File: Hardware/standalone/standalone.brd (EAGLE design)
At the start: 100 x 80 mm, 87 parts, among them Q2 32.768khz, U1 DMS3016SSS-13, U2 DMS3016SSS-13, U3 DMS3016SSS-13, U4 LM2575S-15, U5 NMOS_2N7002, U6 NMOS_2N7002, X1 KUSBVX, X2 KUSBVX

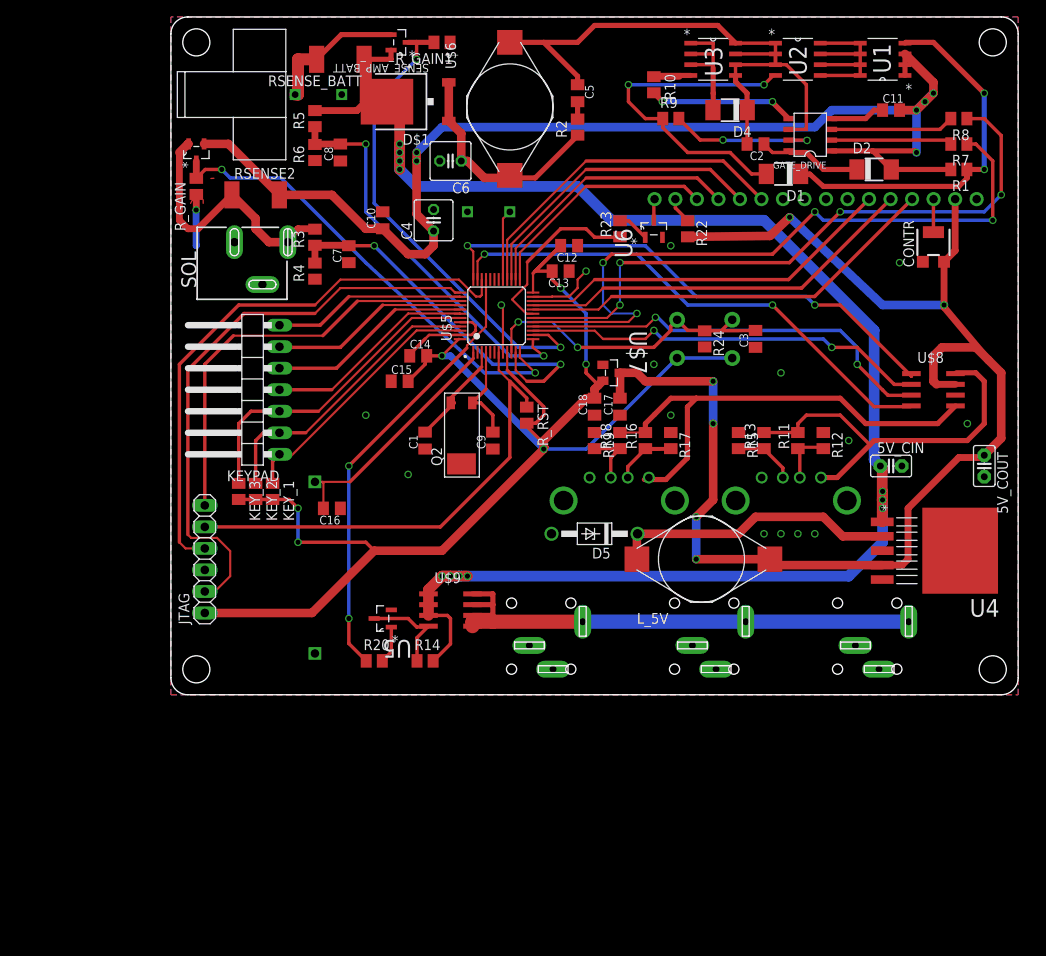
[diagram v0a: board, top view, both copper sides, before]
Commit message: Some Hardware Fixes
Fixed the Battery Connector.
Added more items to ToDo list
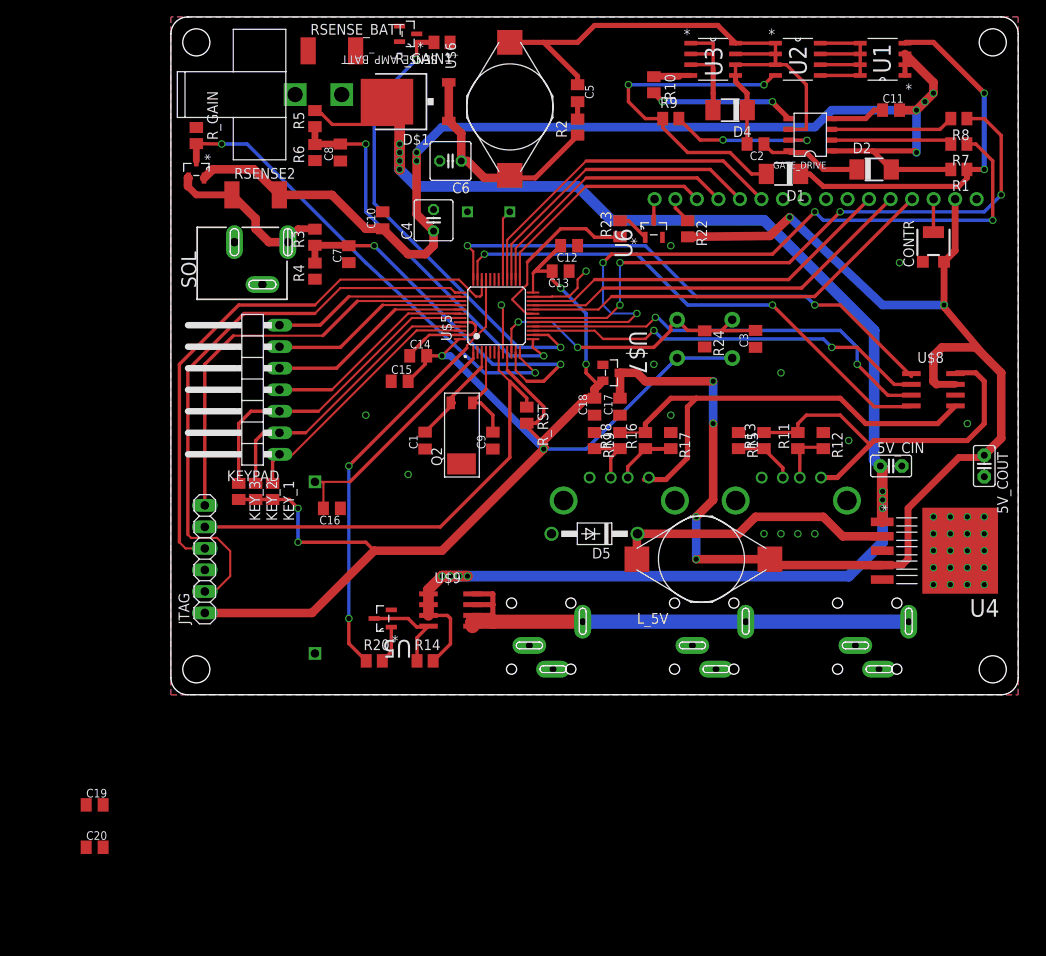
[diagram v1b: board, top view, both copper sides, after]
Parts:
- added C19: 1uF, resistor:C0805K
- added C20: 10uF, resistor:C0805K
- C7: value 0.1uF -> 10uF
- C8: value 0.1uF -> 1uF
- R_GAIN, R_GAIN1: value 10K -> 1k65
- moved R_GAIN 6.00 mm to (3.00, 66.0), turned to 270 degrees
- moved SENSE_AMP_SOL 2.00 mm to (3.00, 62.0), turned to 270 degrees
- moved RSENSE_BATT 1.41 mm to (19.0, 76.0), turned to 0 degrees
- moved SENSE_AMP_BATT 1.41 mm to (28.0, 78.0)
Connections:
- net BATT_I: now also C20.2
- net GND: now also C19.1, C20.1
- net SOL_I: now also C19.2
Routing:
- net N$4: track 16.7 -> 0.00 mm
- net N$16: track 31.5 -> 20.4 mm
- net GND: track 57.0 -> 48.4 mm, vias 16 -> 20
- net V_LOAD: track 195.7 -> 190.7 mm
- net BATT_I: track 57.0 -> 56.0 mm
- net SOL_I: track 55.3 -> 56.2 mm
- net N$9: track 148.4 -> 147.6 mm

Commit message: Cleaned Library and Complete some ToDo list
Added power LED and changed MPPT reverse current diode
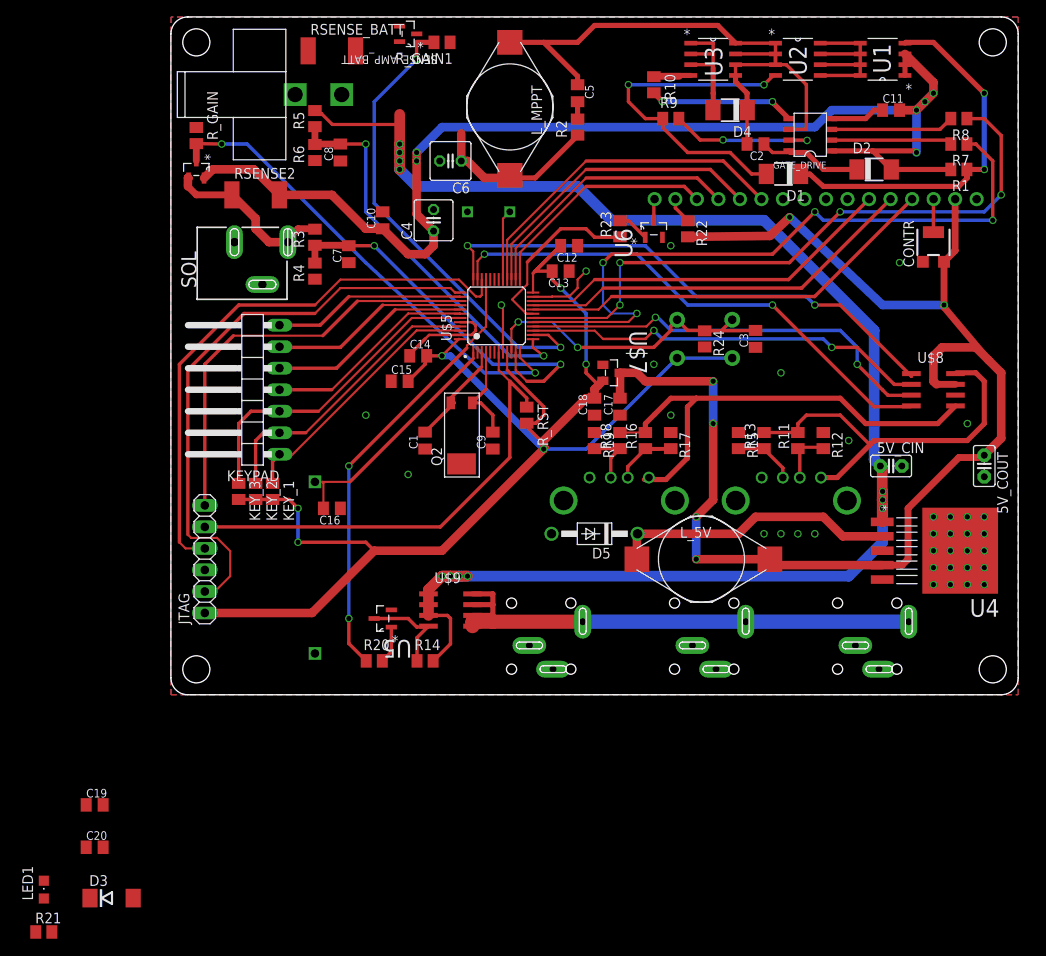
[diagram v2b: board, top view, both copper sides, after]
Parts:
- removed D$1: (no value), equinox:TO252
- removed U$6: 330uF, lib:BOURNS_SDR1806
- added D3: (no value), equinox:DO214AA
- added LED1: (no value), led:CHIPLED_0805
- added L_MPPT: 330u, equinox:BOURNS_SDR1806
- added R21: (no value), resistor:M0805
- L_5V: value 330uF -> 330u; device lib:BOURNS_SDR1806 -> equinox:BOURNS_SDR1806
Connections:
- new net N$37: LED1.C, R21.2
- net +3V3: now also LED1.A
- net GND: now also R21.1
- net N$12: now also D3.A, L_MPPT.P$2; no longer D$1.1, D$1.2, U$6.P$2
- net N$6: now also L_MPPT.P$1; no longer U$6.P$1
- net V_LOAD: now also D3.C; no longer D$1.3
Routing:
- net N$12: track 27.0 -> 20.4 mm
- net V_LOAD: track 190.7 -> 185.6 mm
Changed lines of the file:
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@@
 <layer number="24" name="bOrigins" color="15" fill="1" visible="yes" active="yes"/>
 <layer number="25" name="tNames" color="7" fill="1" visible="yes" active="yes"/>
-<layer number="26" name="bNames" color="7" fill="1" visible="no" active="yes"/>
+<layer number="26" name="bNames" color="7" fill="1" visible="yes" active="yes"/>
 <layer number="27" name="tValues" color="7" fill="1" visible="yes" active="yes"/>
-<layer number="28" name="bValues" color="7" fill="1" visible="no" active="yes"/>
+<layer number="28" name="bValues" color="7" fill="1" visible="yes" active="yes"/>
 <layer number="29" name="tStop" color="7" fill="3" visible="no" active="yes"/>
 <layer number="30" name="bStop" color="7" fill="6" visible="no" active="yes"/>
@@
 <element name="R10" library="rcl" package="M0805" value="5" x="57" y="72" rot="R270"/>
 <element name="C11" library="resistor" package="C0805K" value="1uF" x="85" y="69"/>
-<element name="U$6" library="lib" package="BOURNS_SDR1806" value="330uF" x="40" y="77" rot="R270"/>
+<element name="L_MPPT" library="equinox" package="BOURNS_SDR1806" value="330u" x="40" y="77" rot="R270"/>
 <element name="SENSE_AMP_SOL" library="equinox" package="SOT91P240X110-3N" value="ZXCT1107SA-7" x="3" y="62" smashed="yes" rot="R270">
 <attribute name="PACKAGE" value="SOT-23-3" x="-92" y="102" size="1.778" layer="27" rot="R270" display="off"/>
@@
 </element>
 <element name="D4" library="diode" package="DO-214AC" value="US1D - 1625280" x="66" y="69" rot="R180"/>
-<element name="D$1" library="equinox" package="TO252" value="" x="28" y="70" rot="R90"/>
 <element name="SOL" library="equinox" package="POWER_JACK_SLOT" value="POWER_JACK_2.1MMSLT" x="0" y="56" smashed="yes" rot="R270">
 <attribute name="NAME" x="3" y="48" size="1.778" layer="25" rot="R90"/>
@@
 <attribute name="VALUE" x="79.8428" y="22.5372" size="2.0828" layer="27" ratio="10" rot="SR270"/>
 </element>
-<element name="L_5V" library="lib" package="BOURNS_SDR1806" value="330uF" x="55" y="16">
+<element name="L_5V" library="equinox" package="BOURNS_SDR1806" value="330u" x="55" y="16">
 <attribute name="VERSION" value="0.1" x="55" y="16" size="1.778" layer="27" display="off"/>
 <attribute name="AUTHOR" value="Ashley Grealish" x="55" y="16" size="1.778" layer="27" display="off"/>
@@
 <attribute name="AUTHOR" value="Ashley Grealish" x="-9" y="-18" size="1.778" layer="27" display="off"/>
 </element>
+<element name="D3" library="equinox" package="DO214AA" value="" x="-7" y="-24"/>
+<element name="LED1" library="led" package="CHIPLED_0805" value="" x="-15" y="-23"/>
+<element name="R21" library="resistor" package="M0805" value="" x="-15" y="-28"/>
 </elements>
 <signals>
@@
 <contactref element="C19" pad="1"/>
 <contactref element="C20" pad="1"/>
+<contactref element="R21" pad="1"/>
 <wire x1="88.75" y1="51.1" x2="95.1" y2="58.5" width="0" layer="19" extent="1-1"/>
 <wire x1="86" y1="51" x2="88.75" y2="51.1" width="0" layer="19" extent="1-1"/>
@@
 <wire x1="-10" y1="-13" x2="4" y2="14.73" width="0" layer="19" extent="1-1"/>
 <wire x1="-10" y1="-18" x2="-10" y2="-13" width="0" layer="19" extent="1-1"/>
+<wire x1="-15.95" y1="-28" x2="-10" y2="-18" width="0" layer="19" extent="1-1"/>
 </signal>
 <signal name="N$5">
@@
 <contactref element="C2" pad="2"/>
 <contactref element="C5" pad="1"/>
-<contactref element="U$6" pad="P$1"/>
+<contactref element="L_MPPT" pad="P$1"/>
 <contactref element="GATE_DRIVE" pad="6"/>
 <contactref element="D4" pad="C"/>
@@
 <contactref element="RSENSE_BATT" pad="1"/>
 <contactref element="SENSE_AMP_BATT" pad="3"/>
-<contactref element="D$1" pad="3"/>
 <contactref element="U$9" pad="1"/>
 <contactref element="U$9" pad="3"/>
@@
 <wire x1="34.29" y1="14" x2="34" y2="14" width="1.27" layer="16"/>
 <wire x1="34" y1="14" x2="32" y2="14" width="1.27" layer="16"/>
-<wire x1="27" y1="68.5" x2="25.5" y2="70" width="1.27" layer="1"/>
 <wire x1="27" y1="68.5" x2="27" y2="65" width="1.27" layer="1"/>
 <via x="27" y="62" extent="1-16" drill="0.6"/>
@@
 <wire x1="26.67" y1="67.31" x2="19.05" y2="67.31" width="0.381" layer="1"/>
 <wire x1="17.78" y1="68.58" x2="17" y2="68.95" width="0.381" layer="1"/>
-<wire x1="26.67" y1="67.31" x2="25.5" y2="70" width="0.381" layer="1"/>
-<wire x1="16.2" y1="76" x2="26.984" y2="78.9144" width="0" layer="19" extent="1-1"/>
-<wire x1="25.5" y1="70" x2="16.2" y2="76" width="0" layer="19" extent="1-1"/>
+<contactref element="D3" pad="C"/>
+<wire x1="27" y1="68.5" x2="26.984" y2="78.9144" width="0" layer="19" extent="1-1"/>
+<wire x1="26.67" y1="67.31" x2="27" y2="68.5" width="0" layer="19" extent="1-1"/>
+<wire x1="16.2" y1="76" x2="17" y2="68.95" width="0" layer="19" extent="1-1"/>
+<wire x1="-9.55" y1="-24" x2="30.95" y2="4" width="0" layer="19" extent="1-1"/>
 </signal>
 <signal name="N$12">
-<contactref element="D$1" pad="1"/>
-<contactref element="D$1" pad="2"/>
 <contactref element="R2" pad="1"/>
-<contactref element="U$6" pad="P$2"/>
+<contactref element="L_MPPT" pad="P$2"/>
 <contactref element="C6" pad="1"/>
 <wire x1="48" y1="66.05" x2="48" y2="66" width="0.6096" layer="1"/>
@@
 <wire x1="39.6972" y1="61" x2="40" y2="61.3028" width="1.016" layer="1"/>
 <wire x1="34.27" y1="63" x2="34.27" y2="66.25" width="1.016" layer="1"/>
-<wire x1="34.27" y1="66.25" x2="32.8" y2="67.72" width="1.016" layer="1"/>
-<wire x1="32.8" y1="72.28" x2="32.8" y2="67.72" width="1.016" layer="1"/>
+<contactref element="D3" pad="A"/>
+<wire x1="-4.45" y1="-24" x2="37" y2="61" width="0" layer="19" extent="1-1"/>
 </signal>
 <signal name="USB_OUT2" class="1">
@@
 <wire x1="45" y1="50" x2="45" y2="49" width="0.4064" layer="1"/>
 <wire x1="45" y1="49" x2="46" y2="48" width="0.4064" layer="1"/>
+<contactref element="LED1" pad="A"/>
+<wire x1="4" y1="9.65" x2="-15" y2="-24.05" width="0" layer="19" extent="1-1"/>
 </signal>
 <signal name="+5V">
@@
 <via x="96" y="13" extent="1-16" drill="0.6"/>
 </signal>
+<signal name="N$37">
+<contactref element="LED1" pad="C"/>
+<contactref element="R21" pad="2"/>
+<wire x1="-15" y1="-21.95" x2="-14.05" y2="-28" width="0" layer="19" extent="1-1"/>
+</signal>
 </signals>

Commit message: Many PCB Improvements
Tidied up Silkscreen.
Changed some through hole components to surface mount.
Changed the 15V regulator for 5V as originally intended.
Checked power rating of converters. Need to update 5V out to 3A.
On PCB, tidied up the 12V track and thickened so that it can carry
larger current.
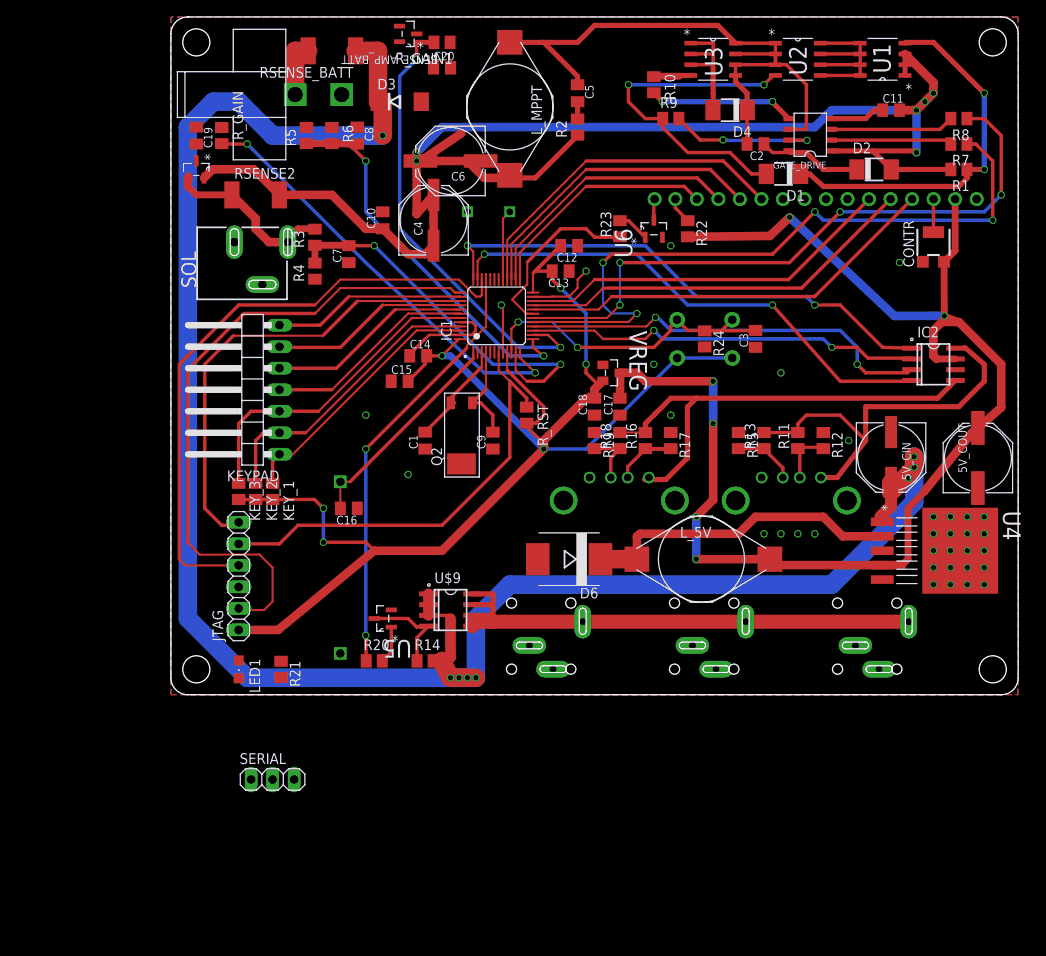
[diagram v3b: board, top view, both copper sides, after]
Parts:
- removed D5: (no value), diode:DO41Z10
- removed U$8: AP1212, equinox:SO8
- added D6: B340-13-F, equinox:SMC
- added IC2: AP1212, equinox:SO8
- added SERIAL: (no value), pinhead:1X03
- 5V_CIN: device capacitor-wima:C2.5-2 -> resistor:PANASONIC_E
- 5V_COUT: device capacitor-wima:C2.5-2 -> resistor:PANASONIC_F
- C4: device resistor:C025-050X050 -> resistor:PANASONIC_E
- C6: device resistor:C025-050X050 -> resistor:PANASONIC_F
- LED1: value (none) -> POW_3V3
- R21: value (none) -> 1K
- U4: value LM2575S-15 -> LM2575S-5
- moved C20 100.7 mm to (32.0, 74.0)
- moved D3 100.0 mm to (27.0, 70.0)
- moved C19 79.9 mm to (3.00, 66.0), turned to 270 degrees
- moved R21 41.8 mm to (13.0, 3.00), turned to 270 degrees
- moved LED1 34.7 mm to (8.00, 3.00), turned to 180 degrees
- moved JTAG 4.47 mm to (8.00, 14.0)
- moved BATT_BCKUP 3.00 mm to (20.0, 15.0)
- moved R_GAIN 3.00 mm to (6.00, 66.0)
- moved C8 2.83 mm to (22.0, 66.0), turned to 270 degrees
- moved R6 2.83 mm to (19.0, 66.0), turned to 270 degrees
- moved R5 2.24 mm to (16.0, 66.0)
- moved C16 2.00 mm to (21.0, 22.0)
- moved 5V_COUT 1.20 mm to (95.2, 27.9), turned to 90 degrees
- moved 5V_CIN 1.00 mm to (85.0, 28.0), turned to 270 degrees
- turned RSENSE_BATT to 180 degrees
- renumbered U$5 to IC1, U$7 to VREG
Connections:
- net +5V: now also 5V_COUT.+, IC2.7; no longer 5V_COUT.1, U$8.7
- net GND: now also 5V_CIN.-, 5V_COUT.-, C4.-, C6.-, D6.A, IC2.6, SERIAL.3; no longer 5V_CIN.2, 5V_COUT.2, C4.2, C6.2, D5.A, U$8.6
- net N$12: now also C6.+; no longer C6.1
- net N$21: now also D6.C; no longer D5.C
- net N$9: now also C4.+; no longer C4.1
- net USART1_RX: now also SERIAL.1
- net USART1_TX: now also SERIAL.2
- net USB_EN1: now also IC2.1; no longer U$8.1
- net USB_EN2: now also IC2.4; no longer U$8.4
- net USB_FLG1: now also IC2.2; no longer U$8.2
- net USB_FLG2: now also IC2.3; no longer U$8.3
- net USB_OUT1: now also IC2.8; no longer U$8.8
- net USB_OUT2: now also IC2.5; no longer U$8.5
- net V_LOAD: now also 5V_CIN.+; no longer 5V_CIN.1
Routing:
- net V_LOAD: track 185.6 -> 232.7 mm, vias 11 -> 8
- net SWCLK: track 68.3 -> 76.5 mm
- net N$12: track 20.4 -> 27.7 mm
- net N$4: track 0.00 -> 6.70 mm
- net SWO: track 49.9 -> 56.5 mm
- net SWDIO: track 66.9 -> 72.9 mm
- net SOL_I: track 56.2 -> 51.1 mm
- net +5V: track 162.5 -> 157.9 mm
- net N$9: track 147.6 -> 152.1 mm
- net N$21: track 33.7 -> 37.9 mm
- net +3V3: track 179.9 -> 176.2 mm
- net NRST: track 56.2 -> 53.1 mm
- net V_BACKUP: track 29.5 -> 26.3 mm
- net BATT_I: track 56.0 -> 53.5 mm
- net USB_EN1: track 63.3 -> 61.6 mm
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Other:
- board text added: "Move Buzzer Swap Solar and Batt Connector"
- board text removed: "INNER BOX DIMENSIONS"
- board text removed: "KEYPAD"
- board text removed: "OUTER BOX DIMENSIONS"

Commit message: Increase 5V Output to 3A max
Switched SMPS Controller, Inductor and Capacitor.
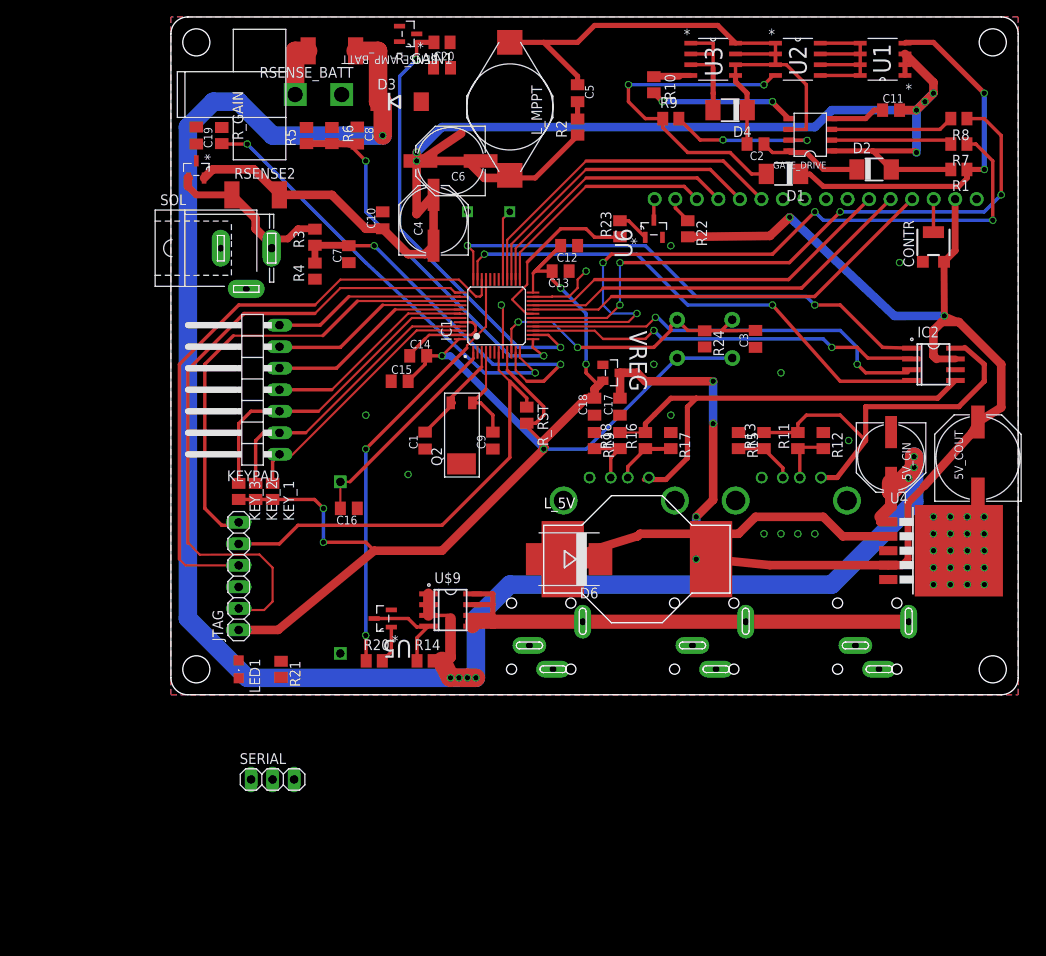
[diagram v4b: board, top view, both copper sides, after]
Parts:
- 5V_COUT: value 330u -> 1000uF; device resistor:PANASONIC_F -> resistor:PANASONIC_G
- L_5V: value 330u -> 100uH; device equinox:BOURNS_SDR1806 -> equinox:INDUC_BOURNS_SDR2207
- L_MPPT: device equinox:BOURNS_SDR1806 -> equinox:INDUC_BOURNS_SDR1806
- SOL: value POWER_JACK_2.1MMSLT -> (none); device equinox:POWER_JACK_SLOT -> con-jack:SPC4077
- U4: value LM2575S-5 -> LM2576S; device equinox:TO170P1435X465-6N -> equinox:TO263-5
- moved SOL 9.48 mm to (8.89, 52.7), turned to 0 degrees
- moved U4 2.54 mm to (90.5, 17.0)
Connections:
- net GND: now also SOL.1, SOL.2; no longer SOL.GND@1, SOL.GND@2
- net N$16: now also SOL.3; no longer SOL.PWR
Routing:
- net N$21: track 37.9 -> 45.2 mm
- net N$16: track 20.4 -> 21.2 mm
- net V_LOAD: track 232.7 -> 233.4 mm
- net +5V: track 157.9 -> 157.4 mm
